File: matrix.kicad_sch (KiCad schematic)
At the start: 208 parts, among them SW10 F7, SW100 RCRTL, SW101 arrow_LT, SW102 arrow_DN, SW103 arrow_RT, SW104 num_0, SW105 num_DEL, SW106 num_ENTER, SW11 F8, SW12 F9, SW13 F10, SW14 F11, SW15 F12, SW16 G1, SW17 `, SW18 1, SW19 2, SW20 3, SW21 4, SW22 5, SW23 6, SW24 7, SW25 8, SW26 9, SW27 0, SW28 -, SW29 =, SW3 esc, SW30 Backspace, SW31 insert, SW32 home, SW33 NUM_lock, SW34 num_/, SW35 num_*, SW36 num_-, SW37 G2, SW38 TAB, SW39 Q, SW4 F1, SW40 W, SW41 E, SW42 R, SW43 T, SW44 Y, SW45 U, SW46 I, SW47 O, SW48 P, SW49 [, SW5 F2, SW50 ], SW51 \, SW52 END, SW53 PGUP, SW54 num_7, SW55 num_8, SW56 num_9, SW57 G3, SW58 CAP_LOCK, SW59 A, SW6 F3, SW60 S, SW61 D, SW62 F, SW63 G, SW64 H, SW65 J, SW66 K, SW67 L, SW68 ;, SW69 ', SW7 F4, SW70 ENTER, SW71 DELETE, SW72 PGDN, SW73 num_4, SW74 num_5, SW75 num_6, SW76 num_+, SW77 G4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

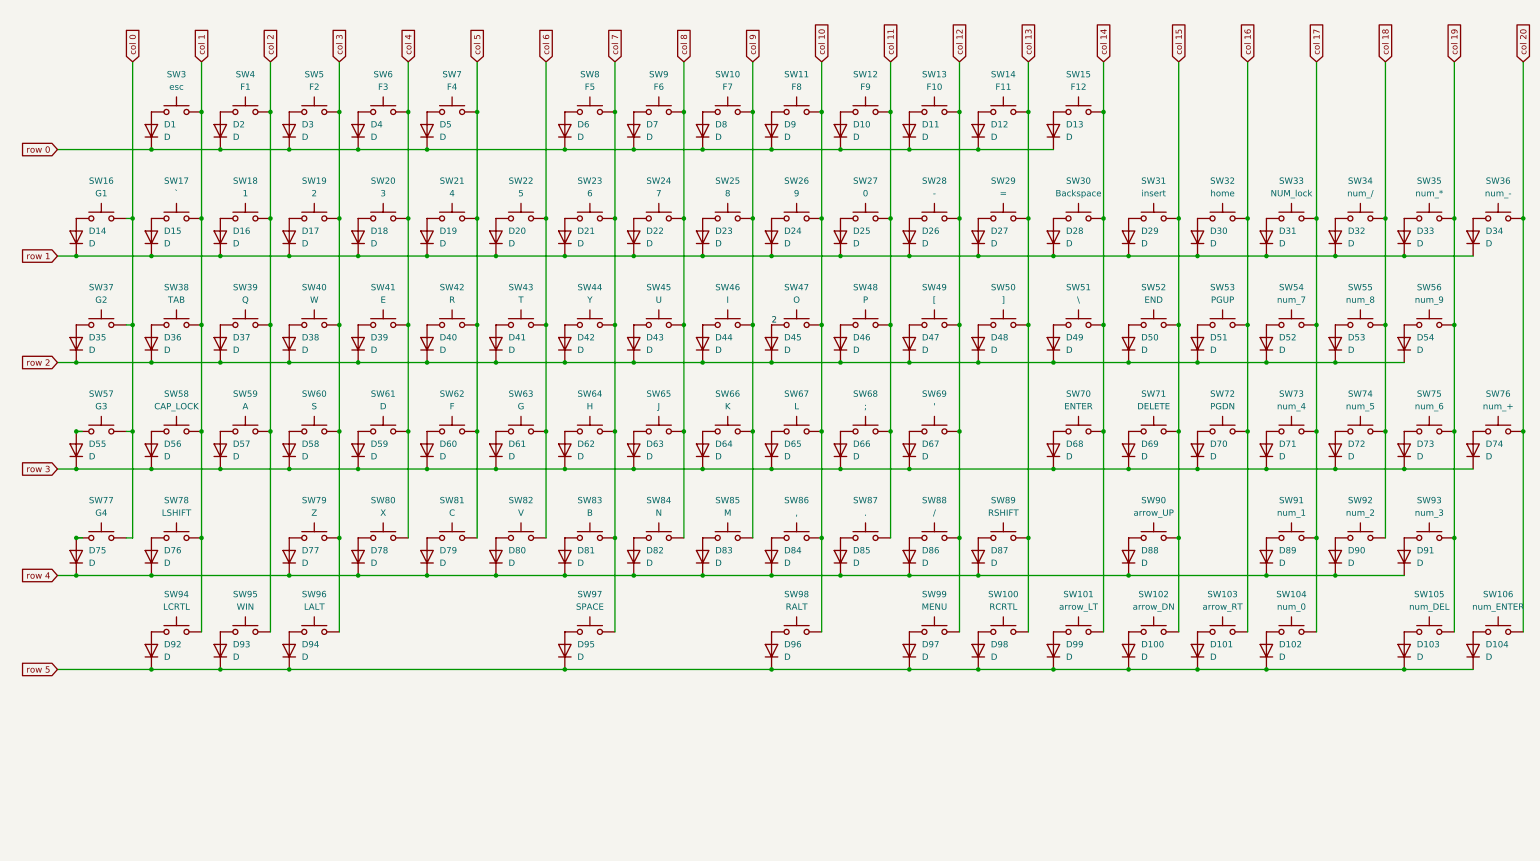
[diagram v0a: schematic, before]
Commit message: Finalization of 89 key
Changed 104 keys to 89, removed LEDs, created files needed for production.
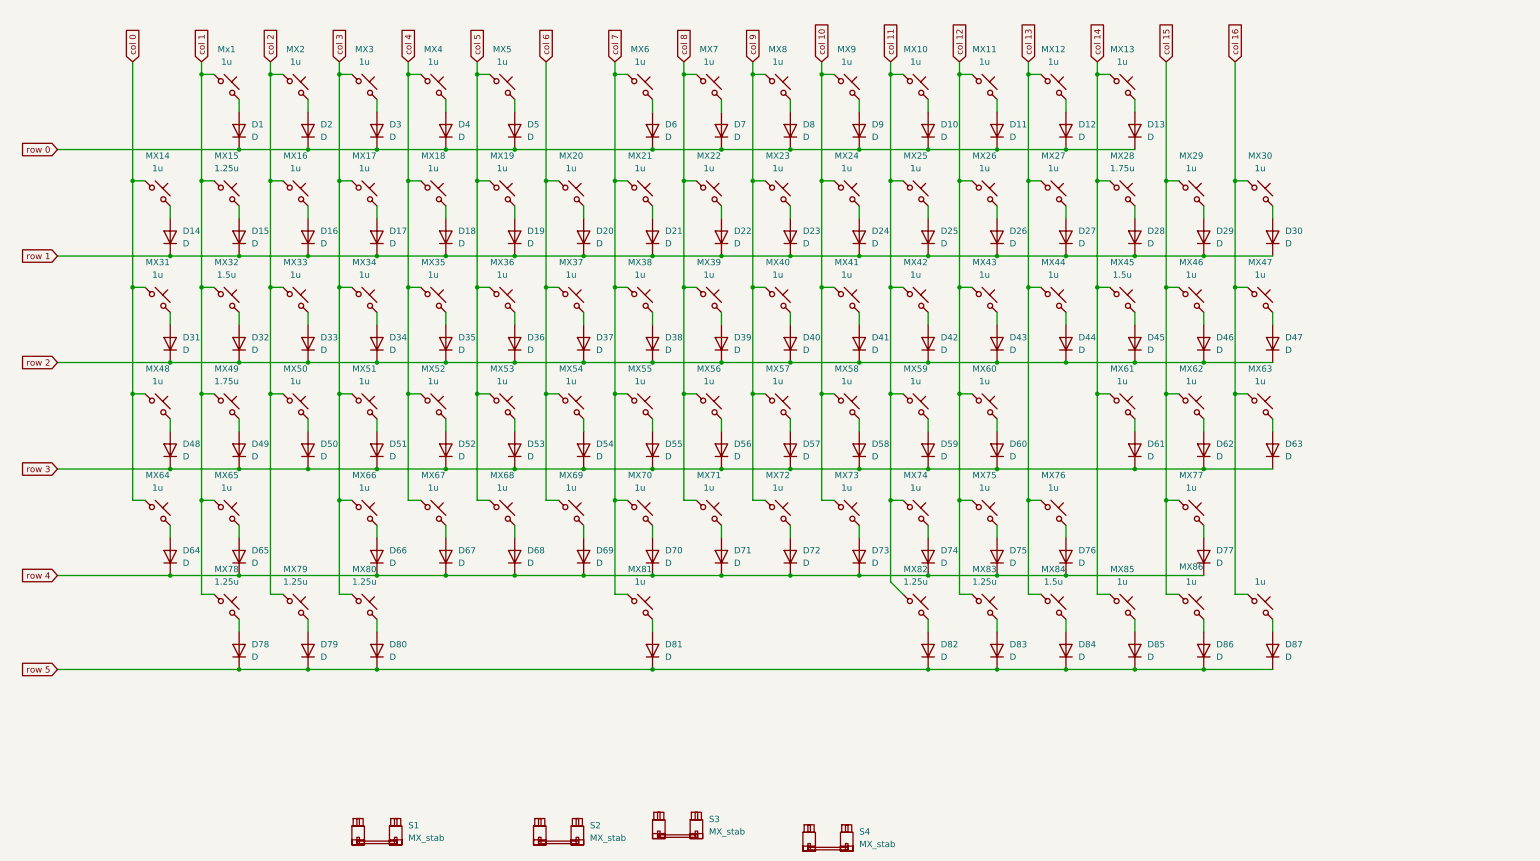
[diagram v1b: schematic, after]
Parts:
- removed D100, D101, D102, D103, D104, D88, D89, D90, D91, D92, D93, D94, D95, D96, D97, D98, D99: D, Diode_SMD:D_SOD-123, symbol Device:D
- removed SW10: F7, Alps_Only:ALPS-1U, symbol Switch:SW_Push
- removed SW100: RCRTL, Alps_Only:ALPS-1.25U, symbol Switch:SW_Push
- removed SW101: arrow_LT, Alps_Only:ALPS-1U, symbol Switch:SW_Push
- removed SW102: arrow_DN, Alps_Only:ALPS-1U, symbol Switch:SW_Push
- removed SW103: arrow_RT, Alps_Only:ALPS-1U, symbol Switch:SW_Push
- removed SW104: num_0, Alps_Only:ALPS-2U, symbol Switch:SW_Push
- removed SW105: num_DEL, Alps_Only:ALPS-1U, symbol Switch:SW_Push
- removed SW106: num_ENTER, Alps_Only:ALPS-2U, symbol Switch:SW_Push
- removed SW11: F8, Alps_Only:ALPS-1U, symbol Switch:SW_Push
- removed SW12: F9, Alps_Only:ALPS-1U, symbol Switch:SW_Push
- removed SW13: F10, Alps_Only:ALPS-1U, symbol Switch:SW_Push
- removed SW14: F11, Alps_Only:ALPS-1U, symbol Switch:SW_Push
- removed SW15: F12, Alps_Only:ALPS-1U, symbol Switch:SW_Push
- removed SW16: G1, Alps_Only:ALPS-1U, symbol Switch:SW_Push
- removed SW17: `, Alps_Only:ALPS-1.25U, symbol Switch:SW_Push
- removed SW18: 1, Alps_Only:ALPS-1U, symbol Switch:SW_Push
- removed SW19: 2, Alps_Only:ALPS-1U, symbol Switch:SW_Push
- removed SW20: 3, Alps_Only:ALPS-1U, symbol Switch:SW_Push
- removed SW21: 4, Alps_Only:ALPS-1U, symbol Switch:SW_Push
- removed SW22: 5, Alps_Only:ALPS-1U, symbol Switch:SW_Push
- removed SW23: 6, Alps_Only:ALPS-1U, symbol Switch:SW_Push
- removed SW24: 7, Alps_Only:ALPS-1U, symbol Switch:SW_Push
- removed SW25: 8, Alps_Only:ALPS-1U, symbol Switch:SW_Push
- removed SW26: 9, Alps_Only:ALPS-1U, symbol Switch:SW_Push
- removed SW27: 0, Alps_Only:ALPS-1U, symbol Switch:SW_Push
- removed SW28: -, Alps_Only:ALPS-1U, symbol Switch:SW_Push
- removed SW29: =, Alps_Only:ALPS-1U, symbol Switch:SW_Push
- removed SW3: esc, Alps_Only:ALPS-1U, symbol Switch:SW_Push
- removed SW30: Backspace, Alps_Only:ALPS-1.75U, symbol Switch:SW_Push
- removed SW31: insert, Alps_Only:ALPS-1U, symbol Switch:SW_Push
- removed SW32: home, Alps_Only:ALPS-1U, symbol Switch:SW_Push
- removed SW33: NUM_lock, Alps_Only:ALPS-1U, symbol Switch:SW_Push
- removed SW34: num_/, Alps_Only:ALPS-1U, symbol Switch:SW_Push
- removed SW35: num_*, Alps_Only:ALPS-1U, symbol Switch:SW_Push
- removed SW36: num_-, Alps_Only:ALPS-1U, symbol Switch:SW_Push
- removed SW37: G2, Alps_Only:ALPS-1U, symbol Switch:SW_Push
- removed SW38: TAB, Alps_Only:ALPS-1.5U, symbol Switch:SW_Push
- removed SW39: Q, Alps_Only:ALPS-1U, symbol Switch:SW_Push
- removed SW4: F1, Alps_Only:ALPS-1U, symbol Switch:SW_Push
- removed SW40: W, Alps_Only:ALPS-1U, symbol Switch:SW_Push
- removed SW41: E, Alps_Only:ALPS-1U, symbol Switch:SW_Push
- removed SW42: R, Alps_Only:ALPS-1U, symbol Switch:SW_Push
- removed SW43: T, Alps_Only:ALPS-1U, symbol Switch:SW_Push
- removed SW44: Y, Alps_Only:ALPS-1U, symbol Switch:SW_Push
- removed SW45: U, Alps_Only:ALPS-1U, symbol Switch:SW_Push
- removed SW46: I, Alps_Only:ALPS-1U, symbol Switch:SW_Push
- removed SW47: O, Alps_Only:ALPS-1U, symbol Switch:SW_Push
- removed SW48: P, Alps_Only:ALPS-1U, symbol Switch:SW_Push
- removed SW49: [, Alps_Only:ALPS-1U, symbol Switch:SW_Push
- removed SW5: F2, Alps_Only:ALPS-1U, symbol Switch:SW_Push
- removed SW50: ], Alps_Only:ALPS-1U, symbol Switch:SW_Push
- removed SW51: \, Alps_Only:ALPS-1.5U, symbol Switch:SW_Push
- removed SW52: END, Alps_Only:ALPS-1U, symbol Switch:SW_Push
- removed SW53: PGUP, Alps_Only:ALPS-1U, symbol Switch:SW_Push
- removed SW54: num_7, Alps_Only:ALPS-1U, symbol Switch:SW_Push
- removed SW55: num_8, Alps_Only:ALPS-1U, symbol Switch:SW_Push
- removed SW56: num_9, Alps_Only:ALPS-1U, symbol Switch:SW_Push
- removed SW57: G3, Alps_Only:ALPS-1U, symbol Switch:SW_Push
- removed SW58: CAP_LOCK, Alps_Only:ALPS-1.75U, symbol Switch:SW_Push
- removed SW59: A, Alps_Only:ALPS-1U, symbol Switch:SW_Push
- removed SW6: F3, Alps_Only:ALPS-1U, symbol Switch:SW_Push
- removed SW60: S, Alps_Only:ALPS-1U, symbol Switch:SW_Push
- removed SW61: D, Alps_Only:ALPS-1U, symbol Switch:SW_Push
- removed SW62: F, Alps_Only:ALPS-1U, symbol Switch:SW_Push
- removed SW63: G, Alps_Only:ALPS-1U, symbol Switch:SW_Push
- removed SW64: H, Alps_Only:ALPS-1U, symbol Switch:SW_Push
- removed SW65: J, Alps_Only:ALPS-1U, symbol Switch:SW_Push
- removed SW66: K, Alps_Only:ALPS-1U, symbol Switch:SW_Push
- removed SW67: L, Alps_Only:ALPS-1U, symbol Switch:SW_Push
- removed SW68: ;, Alps_Only:ALPS-1U, symbol Switch:SW_Push
- removed SW69: ', Alps_Only:ALPS-1U, symbol Switch:SW_Push
- removed SW7: F4, Alps_Only:ALPS-1U, symbol Switch:SW_Push
- removed SW70: ENTER, Alps_Only:ALPS-2.25U, symbol Switch:SW_Push
- removed SW71: DELETE, Alps_Only:ALPS-1U, symbol Switch:SW_Push
- removed SW72: PGDN, Alps_Only:ALPS-1U, symbol Switch:SW_Push
- removed SW73: num_4, Alps_Only:ALPS-1U, symbol Switch:SW_Push
- removed SW74: num_5, Alps_Only:ALPS-1U, symbol Switch:SW_Push
- removed SW75: num_6, Alps_Only:ALPS-1U, symbol Switch:SW_Push
- removed SW76: num_+, Alps_Only:ALPS-2U, symbol Switch:SW_Push
- removed SW77: G4, Alps_Only:ALPS-1U, symbol Switch:SW_Push
- removed SW78: LSHIFT, Alps_Only:ALPS-2.25U, symbol Switch:SW_Push
- removed SW79: Z, Alps_Only:ALPS-1U, symbol Switch:SW_Push
- removed SW8: F5, Alps_Only:ALPS-1U, symbol Switch:SW_Push
- removed SW80: X, Alps_Only:ALPS-1U, symbol Switch:SW_Push
- removed SW81: C, Alps_Only:ALPS-1U, symbol Switch:SW_Push
- removed SW82: V, Alps_Only:ALPS-1U, symbol Switch:SW_Push
- removed SW83: B, Alps_Only:ALPS-1U, symbol Switch:SW_Push
- removed SW84: N, Alps_Only:ALPS-1U, symbol Switch:SW_Push
- removed SW85: M, Alps_Only:ALPS-1U, symbol Switch:SW_Push
- removed SW86: ,, Alps_Only:ALPS-1U, symbol Switch:SW_Push
- removed SW87: ., Alps_Only:ALPS-1U, symbol Switch:SW_Push
- removed SW88: /, Alps_Only:ALPS-1U, symbol Switch:SW_Push
- removed SW89: RSHIFT, Alps_Only:ALPS-2.5U, symbol Switch:SW_Push
- removed SW9: F6, Alps_Only:ALPS-1U, symbol Switch:SW_Push
- removed SW90: arrow_UP, Alps_Only:ALPS-1U, symbol Switch:SW_Push
- removed SW91: num_1, Alps_Only:ALPS-1U, symbol Switch:SW_Push
- removed SW92: num_2, Alps_Only:ALPS-1U, symbol Switch:SW_Push
- removed SW93: num_3, Alps_Only:ALPS-1.25U, symbol Switch:SW_Push
- removed SW94: LCRTL, Alps_Only:ALPS-1.25U, symbol Switch:SW_Push
- removed SW95: WIN, Alps_Only:ALPS-1.25U, symbol Switch:SW_Push
- removed SW96: LALT, Alps_Only:ALPS-1.25U, symbol Switch:SW_Push
- removed SW97: SPACE, Alps_Only:ALPS-6.25U, symbol Switch:SW_Push
- removed SW98: RALT, Alps_Only:ALPS-1.25U, symbol Switch:SW_Push
- removed SW99: MENU, Alps_Only:ALPS-1.25U, symbol Switch:SW_Push
- added MX10, MX11, MX12, MX13, MX14, MX16, MX17, MX18, MX19, MX2, MX20, MX21, MX22, MX23, MX24, MX25, MX26, MX27, MX29, MX3, MX30, MX31, MX33, MX34, MX35, MX36, MX37, MX38, MX39, MX4, MX40, MX41, MX42, MX43, MX44, MX46, MX47, MX48, MX5, MX50, MX51, MX52, MX53, MX54, MX55, MX56, MX57, MX58, MX59, MX6, MX60, MX61, MX62, MX63, MX64, MX65, MX66, MX67, MX68, MX69, MX7, MX70, MX71, MX72, MX73, MX74, MX75, MX76, MX77, MX8, MX81, MX85, MX86, MX87, MX9, Mx1: 1u, PCM_marbastlib-mx:SW_MX_HS_CPG151101S11_1u, symbol PCM_marbastlib-mx:MX_SW_HS_CPG151101S11
- added MX15, MX78, MX79, MX80, MX82, MX83: 1.25u, PCM_marbastlib-mx:SW_MX_HS_CPG151101S11_1.25u, symbol PCM_marbastlib-mx:MX_SW_HS_CPG151101S11
- added MX28, MX49: 1.75u, PCM_marbastlib-mx:SW_MX_HS_CPG151101S11_1.75u, symbol PCM_marbastlib-mx:MX_SW_HS_CPG151101S11
- added MX32, MX45, MX84: 1.5u, PCM_marbastlib-mx:SW_MX_HS_CPG151101S11_1.5u, symbol PCM_marbastlib-mx:MX_SW_HS_CPG151101S11
- added S1: MX_stab, PCM_marbastlib-mx:STAB_MX_P_6.25u, symbol PCM_marbastlib-mx:MX_stab
- added S2, S3, S4: MX_stab, PCM_marbastlib-mx:STAB_MX_P_2.25u, symbol PCM_marbastlib-mx:MX_stab
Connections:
- net col 0: now also MX14.1, MX31.1, MX48.1, MX64.1
- net col 1: now also MX15.1, MX32.1, MX49.1, MX65.1, MX78.1, Mx1.1
- net col 10: now also MX24.1, MX41.1, MX58.1, MX73.1, MX9.1
- net col 11: now also MX10.1, MX25.1, MX42.1, MX59.1, MX74.1, MX82.1
- net col 12: now also MX11.1, MX26.1, MX43.1, MX60.1, MX75.1, MX83.1
- net col 13: now also MX12.1, MX27.1, MX44.1, MX76.1, MX84.1
- net col 14: now also MX13.1, MX28.1, MX45.1, MX61.1, MX85.1
- net col 15: now also MX29.1, MX46.1, MX62.1, MX77.1, MX86.1
- net col 16: now also MX30.1, MX47.1, MX63.1, MX87.1
- net col 2: now also MX16.1, MX2.1, MX33.1, MX50.1, MX79.1
- net col 3: now also MX17.1, MX3.1, MX34.1, MX51.1, MX66.1, MX80.1
- net col 4: now also MX18.1, MX35.1, MX4.1, MX52.1, MX67.1
- net col 5: now also MX19.1, MX36.1, MX5.1, MX53.1, MX68.1
- net col 6: now also MX20.1, MX37.1, MX54.1, MX69.1
- net col 7: now also MX21.1, MX38.1, MX55.1, MX6.1, MX70.1, MX81.1
- net col 8: now also MX22.1, MX39.1, MX56.1, MX7.1, MX71.1
- net col 9: now also MX23.1, MX40.1, MX57.1, MX72.1, MX8.1
- net row 1: no longer D31.1 (K), D32.1 (K), D33.1 (K), D34.1 (K)
- net row 2: now also D31.1 (K), D32.1 (K), D33.1 (K), D34.1 (K); no longer D48.1 (K), D49.1 (K), D50.1 (K), D51.1 (K), D52.1 (K), D53.1 (K), D54.1 (K)
- net row 3: now also D48.1 (K), D49.1 (K), D50.1 (K), D51.1 (K), D52.1 (K), D53.1 (K), D54.1 (K); no longer D64.1 (K), D65.1 (K), D66.1 (K), D67.1 (K), D68.1 (K), D69.1 (K), D70.1 (K), D71.1 (K), D72.1 (K), D73.1 (K), D74.1 (K)
- net row 4: now also D64.1 (K), D65.1 (K), D66.1 (K), D67.1 (K), D68.1 (K), D69.1 (K), D70.1 (K), D71.1 (K), D72.1 (K), D73.1 (K), D74.1 (K); no longer D78.1 (K), D79.1 (K), D80.1 (K), D81.1 (K), D82.1 (K), D83.1 (K), D84.1 (K), D85.1 (K), D86.1 (K), D87.1 (K)
- net row 5: now also D78.1 (K), D79.1 (K), D80.1 (K), D81.1 (K), D82.1 (K), D83.1 (K), D84.1 (K), D85.1 (K), D86.1 (K), D87.1 (K)
- net at D72.2 (A): now also MX72.2
- net at D69.2 (A): now also MX69.2
- net at D67.2 (A): now also MX67.2
- net at D80.2 (A): now also MX80.2
- net at D81.2 (A): now also MX81.2
- net at D79.2 (A): now also MX79.2
- net at D44.2 (A): now also MX44.2
- net at D62.2 (A): now also MX62.2
- net at D31.2 (A): now also MX31.2
- net at D87.2 (A): now also MX87.2
- net at D46.2 (A): now also MX46.2
- net at D77.2 (A): now also MX77.2
- net at D2.2 (A): now also MX2.2
- net at D12.2 (A): now also MX12.2
- net at D41.2 (A): now also MX41.2
- net at D28.2 (A): now also MX28.2
- net at D34.2 (A): now also MX34.2
- net at D55.2 (A): now also MX55.2
- net at D38.2 (A): now also MX38.2
- net at D63.2 (A): now also MX63.2
- net at D49.2 (A): now also MX49.2
- net at D4.2 (A): now also MX4.2
- net at D75.2 (A): now also MX75.2
- net at D10.2 (A): now also MX10.2
- net at D20.2 (A): now also MX20.2
- net at D14.2 (A): now also MX14.2
- net at D53.2 (A): now also MX53.2
- net at D50.2 (A): now also MX50.2
- net at D71.2 (A): now also MX71.2
- net at D59.2 (A): now also MX59.2
- net at D1.2 (A): now also Mx1.2
- net at D58.2 (A): now also MX58.2
- net at D3.2 (A): now also MX3.2
- net at D84.2 (A): now also MX84.2
- net at D78.2 (A): now also MX78.2
- net at D42.2 (A): now also MX42.2
- net at D9.2 (A): now also MX9.2
- net at D30.2 (A): now also MX30.2
- net at D60.2 (A): now also MX60.2
- net at D13.2 (A): now also MX13.2
- net at D86.2 (A): now also MX86.2
- net at D47.2 (A): now also MX47.2
- net at D11.2 (A): now also MX11.2
- net at D16.2 (A): now also MX16.2
- net at D32.2 (A): now also MX32.2
- net at D64.2 (A): now also MX64.2
- net at D24.2 (A): now also MX24.2
- net at D21.2 (A): now also MX21.2
- net at D29.2 (A): now also MX29.2
- net at D40.2 (A): now also MX40.2
- net at D51.2 (A): now also MX51.2
- net at D83.2 (A): now also MX83.2
- net at D19.2 (A): now also MX19.2
- net at D61.2 (A): now also MX61.2
- net at D66.2 (A): now also MX66.2
- net at D52.2 (A): now also MX52.2
- net at D82.2 (A): now also MX82.2
- net at D27.2 (A): now also MX27.2
- net at D74.2 (A): now also MX74.2
- net at D17.2 (A): now also MX17.2
- net at D36.2 (A): now also MX36.2
- net at D37.2 (A): now also MX37.2
- net at D23.2 (A): now also MX23.2
- net at D26.2 (A): now also MX26.2
- net at D68.2 (A): now also MX68.2
- net at D48.2 (A): now also MX48.2
- net at D85.2 (A): now also MX85.2
- net at D35.2 (A): now also MX35.2
- net at D5.2 (A): now also MX5.2
- net at D7.2 (A): now also MX7.2
- net at D70.2 (A): now also MX70.2
- net at D76.2 (A): now also MX76.2
- net at D6.2 (A): now also MX6.2
- net at D39.2 (A): now also MX39.2
- net at D73.2 (A): now also MX73.2
- net at D65.2 (A): now also MX65.2
- net at D15.2 (A): now also MX15.2
- net at D8.2 (A): now also MX8.2
- net at D57.2 (A): now also MX57.2
- net at D56.2 (A): now also MX56.2
- net at D54.2 (A): now also MX54.2
- net at D25.2 (A): now also MX25.2
- net at D18.2 (A): now also MX18.2
- net at D22.2 (A): now also MX22.2
- net at D43.2 (A): now also MX43.2
- net at D33.2 (A): now also MX33.2
- net 2: no longer names the net of D45.2 (A)
- net 2: now also MX45.2
